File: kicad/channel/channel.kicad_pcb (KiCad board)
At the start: 2 copper layers, 53.3 x 43.2 mm, 34 parts, among them J1 Conn_01x07_Male, J2 Conn_01x01_Male, J3 Conn_01x01_Male, J4 Conn_01x01_Male, J5 Conn_01x01_Male, Q1 BC846B, Q2 IRF3205, Q3 IRF3205, Q4 BC846B, Q5 IRF3205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

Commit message: work on kicad
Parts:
- added R17: 10k, Resistor_SMD:R_1206_3216Metric, F.Cu at (157.5, 93.3)
- added R18: 10k, Resistor_SMD:R_1206_3216Metric, F.Cu at (156.8, 79.4)
- added R19: 2.2k, Resistor_SMD:R_1206_3216Metric, F.Cu at (159.4, 100.3)
- added R20: 2.2k, Resistor_SMD:R_1206_3216Metric, F.Cu at (181.6, 75.1)
- C5, C6: value 10u -> 1u; footprint Capacitor_SMD:CP_Elec_6.3x7.7 -> Capacitor_SMD:C_0603_1608Metric
- R10, R11, R2, R3: value 47k -> 22k
- moved C6 22.9 mm to (160.0, 82.1)
- moved C5 19.6 mm to (158.1, 90.8)
- moved R14 11.4 mm to (175.3, 81.3), turned to 180 degrees
- moved R6 11.1 mm to (171.4, 105.4)
- moved Q1 9.53 mm to (163.8, 104.8), turned to 180 degrees
- moved R2 7.18 mm to (168.3, 85.1), turned to 180 degrees
- moved R12 5.68 mm to (165.7, 78.7), turned to 90 degrees
- moved R9 4.96 mm to (154.9, 97.2)
- moved R1 3.42 mm to (170.2, 78.7)
- moved R10 2.84 mm to (162.6, 78.7)
- moved R8 2.54 mm to (170.2, 99.1)
- moved C4 2.29 mm to (155.6, 74.9), turned to -90 degrees
- moved Q4 1.91 mm to (176.5, 74.9), turned to 90 degrees
- moved R4 0.83 mm to (168.3, 88.9)
- moved R13 0.63 mm to (162.6, 88.9)
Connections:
- C5 pad 1: Net-(C5-Pad1) -> Net-(R2-Pad2)
- C5 pad 2: GND -> Net-(C5-Pad2)
- C6 pad 1: Net-(C6-Pad1) -> Net-(R10-Pad2)
- C6 pad 2: GND -> Net-(C6-Pad2)
- Q1 pad 2: GND -> Net-(Q1-Pad2)
- Q2 pad 1: Net-(C6-Pad1) -> Net-(Q2-Pad1)
- Q4 pad 2: GND -> Net-(Q4-Pad2)
- Q5 pad 1: Net-(C5-Pad1) -> Net-(R1-Pad1)
- R1 pad 1: Net-(C5-Pad1) -> Net-(R1-Pad1)
- R14 pad 2: Net-(C5-Pad1) -> Net-(R1-Pad1)
- R6 pad 2: Net-(C6-Pad1) -> Net-(Q2-Pad1)
- R9 pad 1: Net-(C6-Pad1) -> Net-(Q2-Pad1)
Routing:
- net Net-(Q2-Pad1): track 0.00 -> 45.3 mm
- net Net-(C5-Pad1): track 43.7 -> 0.00 mm
- net Net-(C6-Pad1): track 41.0 -> 0.00 mm
- net Net-(R1-Pad1): track 0.00 -> 38.4 mm
- net GND: track 108.4 -> 78.2 mm
- net ref: track 37.3 -> 58.0 mm
- net Net-(R1-Pad2): track 11.7 -> 22.0 mm
- net Net-(R10-Pad2): track 9.20 -> 19.5 mm
- net Net-(Q5-Pad3): track 42.2 -> 33.9 mm
- net Net-(Q4-Pad2): track 0.00 -> 7.85 mm
- net Net-(Q1-Pad2): track 0.00 -> 6.49 mm
- net Net-(C5-Pad2): track 0.00 -> 5.27 mm
- net Net-(C6-Pad2): track 0.00 -> 3.25 mm
- net Net-(Q2-Pad3): track 49.9 -> 47.3 mm
- net Net-(R9-Pad2): track 5.48 -> 8.00 mm
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
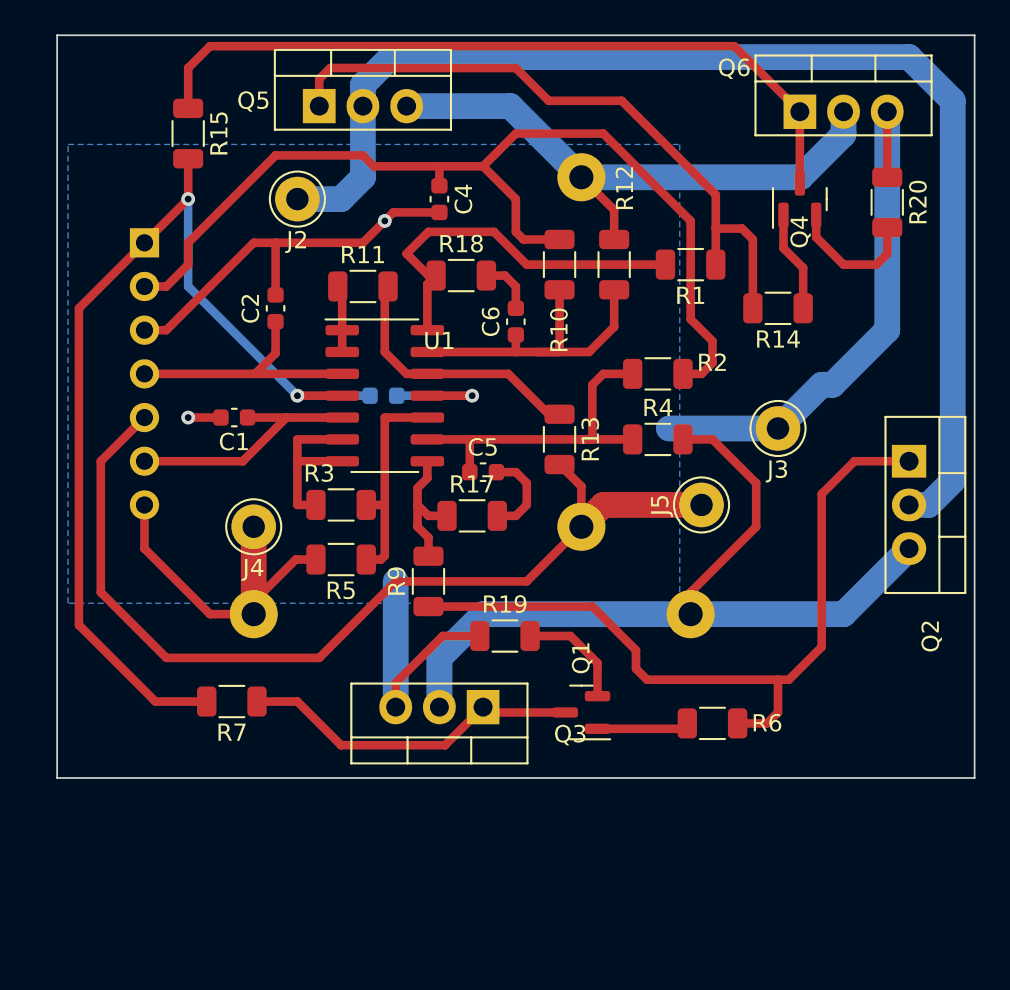
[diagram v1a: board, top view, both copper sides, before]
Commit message: rework PINS, get SD Card working
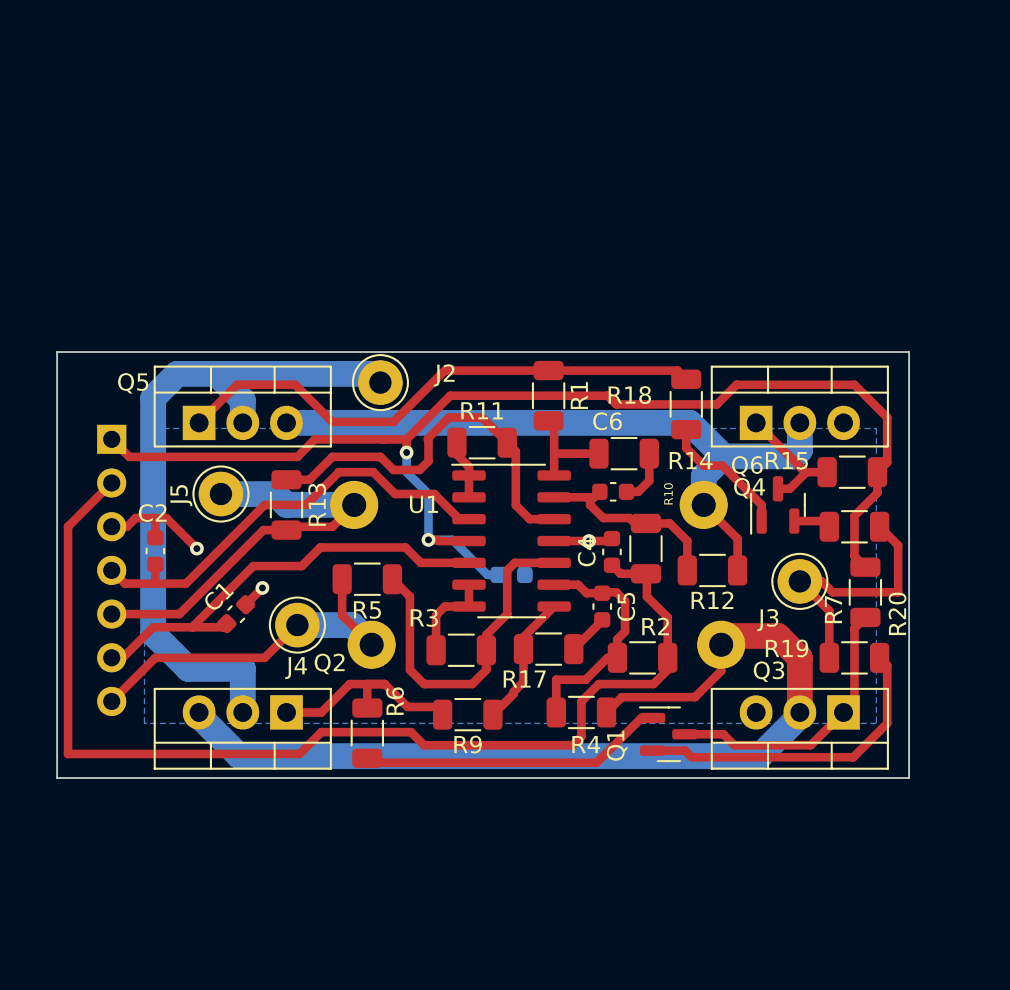
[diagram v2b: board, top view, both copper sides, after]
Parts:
- R8: footprint Resistor_THT:R_Axial_DIN0614_L14.3mm_D5.7mm_P25.40mm_Horizontal -> Resistor_THT:R_Axial_DIN0614_L14.3mm_D5.7mm_P20.32mm_Horizontal
- moved R15 43.3 mm to (179.6, 90.8), turned to 0 degrees
- moved Q2 39.0 mm to (146.7, 104.8), turned to 180 degrees
- moved R7 37.4 mm to (180.3, 97.8), turned to 90 degrees
- moved J5 27.9 mm to (142.9, 92.1)
- moved C4 22.8 mm to (165.6, 95.4), turned to 90 degrees
- moved Q3 21.0 mm to (179.1, 104.8)
- moved R19 20.4 mm to (179.7, 101.6)
- moved R16 20.3 mm to (170.9, 92.7), turned to 180 degrees
- moved R6 20.1 mm to (151.4, 106.0), turned to 90 degrees
- moved Q5 19.7 mm to (141.6, 87.9)
- moved R20 19.0 mm to (179.7, 94.0), turned to 180 degrees
- moved R12 18.7 mm to (171.4, 96.5), turned to 0 degrees
- moved Q6 18.3 mm to (174.0, 87.9)
- moved Q4 17.8 mm to (175.3, 92.7)
- moved R10 17.3 mm to (167.6, 95.2), turned to 90 degrees
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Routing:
- net GND: track 78.2 -> 27.2 mm
- net Net-(Q4-Pad3): track 44.2 -> 8.72 mm
- net Net-(Q2-Pad1): track 45.3 -> 12.7 mm
- net +5V: track 70.9 -> 39.8 mm
- net U1: track 55.5 -> 24.7 mm
- net Net-(R1-Pad2): track 22.0 -> 5.96 mm
- net Net-(Q1-Pad1): track 5.35 -> 17.8 mm
- net Net-(Q1-Pad2): track 6.49 -> 18.6 mm
- net +12V: track 60.0 -> 72.0 mm
- net IN2: track 14.8 -> 25.9 mm
- net IN1: track 15.0 -> 26.1 mm
- net Net-(Q2-Pad3): track 47.3 -> 54.9 mm
- net Net-(C6-Pad1): track 19.5 -> 12.1 mm
- net Net-(R3-Pad2): track 12.8 -> 20.0 mm
- net Net-(R11-Pad2): track 15.5 -> 22.8 mm
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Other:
- board size 53.3 x 43.2 mm -> 49.5 x 24.8 mm
- board text removed: "B1"
- board text removed: "B2"

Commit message: work on kicad
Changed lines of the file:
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@@
     (pad_to_mask_clearance 0)
     (pcbplotparams
-      (layerselection 0x00010fc_ffffffff)
+      (layerselection 0x0000000_ffffffff)
       (disableapertmacros false)
       (usegerberextensions false)
@@
       (effects (font (size 1 1) (thickness 0.15)))
     )
-    (fp_text value "2.2k" (at 0 1.82) (layer "F.Fab")
+    (fp_text value "2.2k" (at 2.54 -0.635 270) (layer "F.Fab")
       (effects (font (size 1 1) (thickness 0.15)))
     )
@@
     (fp_line (start 1.6 -0.8) (end 1.6 0.8) (layer "F.Fab") (width 0.1))
     (fp_line (start -1.6 -0.8) (end 1.6 -0.8) (layer "F.Fab") (width 0.1))
-    (pad "1" smd roundrect (at -1.4625 0) (size 1.125 1.75) (layers "F.Cu" "F.Paste" "F.Mask") (roundrect_rratio 0.222222)
+    (pad "1" smd roundrect (at -1.4625 0) (size 1.125 1.75) (layers "F.Cu" "F.Paste" "F.Mask") (roundrect_rratio 0.2222222222)
       (net 3 "GND") (pintype "passive"))
-    (pad "2" smd roundrect (at 1.4625 0) (size 1.125 1.75) (layers "F.Cu" "F.Paste" "F.Mask") (roundrect_rratio 0.222222)
+    (pad "2" smd roundrect (at 1.4625 0) (size 1.125 1.75) (layers "F.Cu" "F.Paste" "F.Mask") (roundrect_rratio 0.2222222222)
       (net 25 "Net-(Q1-Pad2)") (pintype "passive"))
     (model "${KICAD6_3DMODEL_DIR}/Resistor_SMD.3dshapes/R_1206_3216Metric.wrl"
@@
       (effects (font (size 1 1) (thickness 0.15)))
     )
-    (fp_text value "LM324" (at 3.175 0.635 90) (layer "F.Fab")
+    (fp_text value "LM324" (at -3.56 0.4875 90) (layer "F.Fab")
       (effects (font (size 1 1) (thickness 0.15)))
     )
@@
       (effects (font (size 1 1) (thickness 0.15)))
     )
-    (fp_text value "10k" (at 0 1.82) (layer "F.Fab")
+    (fp_text value "10k" (at -0.5775 -1.4625) (layer "F.Fab")
       (effects (font (size 1 1) (thickness 0.15)))
     )
@@
     (fp_line (start 1.6 -0.8) (end 1.6 0.8) (layer "F.Fab") (width 0.1))
     (fp_line (start -1.6 -0.8) (end 1.6 -0.8) (layer "F.Fab") (width 0.1))
-    (pad "1" smd roundrect (at -1.4625 0) (size 1.125 1.75) (layers "F.Cu" "F.Paste" "F.Mask") (roundrect_rratio 0.222222)
+    (pad "1" smd roundrect (at -1.4625 0) (size 1.125 1.75) (layers "F.Cu" "F.Paste" "F.Mask") (roundrect_rratio 0.2222222222)
       (net 8 "Net-(R1-Pad2)") (pintype "passive"))
-    (pad "2" smd roundrect (at 1.4625 0) (size 1.125 1.75) (layers "F.Cu" "F.Paste" "F.Mask") (roundrect_rratio 0.222222)
+    (pad "2" smd roundrect (at 1.4625 0) (size 1.125 1.75) (layers "F.Cu" "F.Paste" "F.Mask") (roundrect_rratio 0.2222222222)
       (net 24 "Net-(C6-Pad2)") (pintype "passive"))
     (model "${KICAD6_3DMODEL_DIR}/Resistor_SMD.3dshapes/R_1206_3216Metric.wrl"
@@
       (effects (font (size 1 1) (thickness 0.15)))
     )
-    (fp_text value "22k" (at 3.81 0) (layer "F.Fab")
+    (fp_text value "22k" (at -3.175 0) (layer "F.Fab")
       (effects (font (size 1 1) (thickness 0.15)))
     )
@@
       (effects (font (size 1 1) (thickness 0.15)))
     )
-    (fp_text value "BC846B" (at 4.445 0 90) (layer "F.Fab")
+    (fp_text value "BC846B" (at 1.905 -0.635 180) (layer "F.Fab")
       (effects (font (size 1 1) (thickness 0.15)))
     )
@@
       (effects (font (size 1 1) (thickness 0.15)))
     )
-    (fp_text value "10k" (at 1.4625 -0.0275) (layer "F.Fab")
-      (effects (font (size 1 1) (thickness 0.15)))
-    )
-    (fp_text user "${REFERENCE}" (at 4.064 0.889) (layer "F.Fab")
+    (fp_text value "10k" (at 3.302 0 90) (layer "F.Fab")
+      (effects (font (size 1 1) (thickness 0.15)))
+    )
+    (fp_text user "${REFERENCE}" (at 0.127 0) (layer "F.Fab")
       (effects (font (size 0.8 0.8) (thickness 0.12)))
     )
@@
       (effects (font (size 1 1) (thickness 0.15)))
     )
-    (fp_text value "22k" (at 3.175 0) (layer "F.Fab")
+    (fp_text value "22k" (at -3.1175 1.0775) (layer "F.Fab")
       (effects (font (size 1 1) (thickness 0.15)))
     )
@@
       (effects (font (size 1 1) (thickness 0.15)))
     )
-    (fp_text value "IRF3205" (at 2.54 2.5) (layer "F.Fab")
+    (fp_text value "IRF3205" (at 3.175 -0.635) (layer "F.Fab")
       (effects (font (size 1 1) (thickness 0.15)))
     )
@@
       (effects (font (size 1 1) (thickness 0.15)))
     )
-    (fp_text value "1u" (at 0 1.43 90) (layer "F.Fab")
+    (fp_text value "1u" (at 0 -1.778 90) (layer "F.Fab")
       (effects (font (size 1 1) (thickness 0.15)))
     )
@@
       (effects (font (size 1 1) (thickness 0.15)))
     )
-    (fp_text value "IRF3205" (at 2.54 2.5) (layer "F.Fab")
-      (effects (font (size 1 1) (thickness 0.15)))
-    )
-    (fp_text user "${REFERENCE}" (at 1.27 11.2375) (layer "F.Fab")
+    (fp_text value "IRF3205" (at 2.54 0.325) (layer "F.Fab")
+      (effects (font (size 1 1) (thickness 0.15)))
+    )
+    (fp_text user "${REFERENCE}" (at 6.35 -0.95) (layer "F.Fab")
       (effects (font (size 1 1) (thickness 0.15)))
     )
@@
       (effects (font (size 1 1) (thickness 0.15)))
     )
-    (fp_text value "22k" (at -3.175 -0.635) (layer "F.Fab")
+    (fp_text value "22k" (at -3.175 0) (layer "F.Fab")
       (effects (font (size 1 1) (thickness 0.15)))
     )
@@
     (fp_line (start -1.6 -0.8) (end 1.6 -0.8) (layer "F.Fab") (width 0.1))
     (fp_line (start 1.6 0.8) (end -1.6 0.8) (layer "F.Fab") (width 0.1))
-    (pad "1" smd roundrect (at -1.4625 0) (size 1.125 1.75) (layers "F.Cu" "F.Paste" "F.Mask") (roundrect_rratio 0.222222)
+    (pad "1" smd roundrect (at -1.4625 0) (size 1.125 1.75) (layers "F.Cu" "F.Paste" "F.Mask") (roundrect_rratio 0.2222222222)
       (net 28 "Net-(R17-Pad1)") (pintype "passive"))
-    (pad "2" smd roundrect (at 1.4625 0) (size 1.125 1.75) (layers "F.Cu" "F.Paste" "F.Mask") (roundrect_rratio 0.222222)
+    (pad "2" smd roundrect (at 1.4625 0) (size 1.125 1.75) (layers "F.Cu" "F.Paste" "F.Mask") (roundrect_rratio 0.2222222222)
       (net 23 "Net-(C5-Pad2)") (pintype "passive"))
     (model "${KICAD6_3DMODEL_DIR}/Resistor_SMD.3dshapes/R_1206_3216Metric.wrl"
@@
       (effects (font (size 1 1) (thickness 0.15)))
     )
-    (fp_text value "10k" (at 0 1.82 90) (layer "F.Fab")
+    (fp_text value "10k" (at 0.508 -2.286 90) (layer "F.Fab")
       (effects (font (size 1 1) (thickness 0.15)))
     )
@@
       (effects (font (size 1 1) (thickness 0.15)))
     )
-    (fp_text value "10k" (at -3.81 0) (layer "F.Fab")
+    (fp_text value "10k" (at -0.381 -2.032) (layer "F.Fab")
       (effects (font (size 1 1) (thickness 0.15)))
     )
@@
       (effects (font (size 1 1) (thickness 0.15)))
     )
-    (fp_text value "2.2k" (at 0 1.82) (layer "F.Fab")
+    (fp_text value "2.2k" (at -2.54 0 90) (layer "F.Fab")
       (effects (font (size 1 1) (thickness 0.15)))
     )
@@
     (fp_line (start 1.6 -0.8) (end 1.6 0.8) (layer "F.Fab") (width 0.1))
     (fp_line (start -1.6 0.8) (end -1.6 -0.8) (layer "F.Fab") (width 0.1))
-    (pad "1" smd roundrect (at -1.4625 0 180) (size 1.125 1.75) (layers "F.Cu" "F.Paste" "F.Mask") (roundrect_rratio 0.222222)
+    (pad "1" smd roundrect (at -1.4625 0 180) (size 1.125 1.75) (layers "F.Cu" "F.Paste" "F.Mask") (roundrect_rratio 0.2222222222)
       (net 3 "GND") (pintype "passive"))
-    (pad "2" smd roundrect (at 1.4625 0 180) (size 1.125 1.75) (layers "F.Cu" "F.Paste" "F.Mask") (roundrect_rratio 0.222222)
+    (pad "2" smd roundrect (at 1.4625 0 180) (size 1.125 1.75) (layers "F.Cu" "F.Paste" "F.Mask") (roundrect_rratio 0.2222222222)
       (net 27 "Net-(Q4-Pad2)") (pintype "passive"))
     (model "${KICAD6_3DMODEL_DIR}/Resistor_SMD.3dshapes/R_1206_3216Metric.wrl"
@@
       (effects (font (size 1 1) (thickness 0.15)))
     )
-    (fp_text user "${REFERENCE}" (at 3.175 -1.52 90) (layer "F.Fab")
+    (fp_text user "${REFERENCE}" (at 1.905 1.3275 90) (layer "F.Fab")
       (effects (font (size 0.8 0.8) (thickness 0.12)))
     )
@@
       (effects (font (size 1 1) (thickness 0.15)))
     )
-    (fp_text value "BC846B" (at -1.905 -2.54 90) (layer "F.Fab")
+    (fp_text value "BC846B" (at -1.905 0 90) (layer "F.Fab")
       (effects (font (size 1 1) (thickness 0.15)))
     )
@@
       (effects (font (size 1 1) (thickness 0.15)) (justify mirror))
     )
-    (fp_text value "1u" (at 0 -1.43) (layer "B.Fab")
+    (fp_text value "1u" (at -2.286 -0.254) (layer "B.Fab")
       (effects (font (size 1 1) (thickness 0.15)) (justify mirror))
     )
@@
       (effects (font (size 1 1) (thickness 0.15)) (justify mirror))
     )
-    (fp_text value "0.22" (at 8.3125 -5.4325) (layer "B.Fab")
+    (fp_text value "0.22" (at 9.398 -3.937) (layer "B.Fab")
       (effects (font (size 1 1) (thickness 0.15)) (justify mirror))
     )
-    (fp_text user "${REFERENCE}" (at 6.7925 -4.6375) (layer "B.Fab")
+    (fp_text user "${REFERENCE}" (at 4.953 -3.937) (layer "B.Fab")
       (effects (font (size 1 1) (thickness 0.15)) (justify mirror))
     )
@@
       (effects (font (size 1 1) (thickness 0.15)) (justify mirror))
     )
-    (fp_text value "0.22" (at 6.7925 -8.6075) (layer "B.Fab")
+    (fp_text value "0.22" (at 10.922 1.905) (layer "B.Fab")
       (effects (font (size 1 1) (thickness 0.15)) (justify mirror))
     )
-    (fp_text user "${REFERENCE}" (at 6.7925 -4.6375) (layer "B.Fab")
+    (fp_text user "${REFERENCE}" (at 7.112 3.81) (layer "B.Fab")
       (effects (font (size 1 1) (thickness 0.15)) (justify mirror))
     )
